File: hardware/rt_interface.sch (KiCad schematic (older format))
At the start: 51 parts, among them Q1 NTMFS5C682NL, Q2 NTMFS5C682NL, U1 NCS213, U2 MAX44246, U3 LM5109BSD

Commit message: Layout almost complete. Just needs a tidy.
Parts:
- removed JP1: SolderJumper_2_Open, station:SolderJumper-2_6A, symbol Jumper:SolderJumper_2_Open
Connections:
- net +V_PWR: now reaches C12.1, C13.1, C14.1, C15.1, C18.1, Q1.5 (D)
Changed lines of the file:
@@
 $Descr A4 11693 8268
 encoding utf-8
-Sheet 2 5
+Sheet 5 5
 Title ""
 Date ""
@@
 	7450 6100 7800 6100
 Connection ~ 7800 6100
-$Comp
-L power:+BATT #PWR013
-U 1 1 5EA17F06
-P 7450 3400
-AR Path="/5EA10576/5EA17F06" Ref="#PWR013"  Part="1"
-AR Path="/5EEA69D8/5EA17F06" Ref="#PWR?"  Part="1"
-AR Path="/5F6BFC9B/5EA17F06" Ref="#PWR?"  Part="1"
-AR Path="/5EFF2C78/5EA17F06" Ref="#PWR029"  Part="1"
-F 0 "#PWR029" H 7450 3250 50  0001 C CNN
-F 1 "+BATT" H 7465 3573 50  0000 C CNN
-F 2 "" H 7450 3400 50  0001 C CNN
-F 3 "" H 7450 3400 50  0001 C CNN
-	1    7450 3400
-	1    0    0    -1
-$EndComp
 $Comp
 L Device:C C12
@@
 	1300 1350 1300 1400
 Connection ~ 1300 1350
-$Comp
-L Jumper:SolderJumper_2_Open JP1
-U 1 1 5EEB1D69
-P 7450 3600
-AR Path="/5EA10576/5EEB1D69" Ref="JP1"  Part="1"
-AR Path="/5F6BFC9B/5EEB1D69" Ref="JP?"  Part="1"
-AR Path="/5EFF2C78/5EEB1D69" Ref="JP4"  Part="1"
-F 0 "JP4" V 7450 3668 50  0000 L CNN
-F 1 "SolderJumper_2_Open" V 7495 3668 50  0001 L CNN
-F 2 "station:SolderJumper-2_6A" H 7450 3600 50  0001 C CNN
-F 3 "~" H 7450 3600 50  0001 C CNN
-	1    7450 3600
-	0    1    1    0
-$EndComp
 Wire Wire Line
 	7450 3750 7450 3800
-Wire Wire Line
-	7450 3400 7450 3450
 $Comp
 L Device:C C17
@@
 Text Label 9700 5700 0    50   ~ 0
 SHUNT-
+$Comp
+L Station:+V_PWR #PWR051
+U 1 1 606EBBA2
+P 7450 3750
+AR Path="/5EFF2C78/606EBBA2" Ref="#PWR051"  Part="1"
+AR Path="/5EA10576/606EBBA2" Ref="#PWR050"  Part="1"
+F 0 "#PWR051" H 7450 3600 50  0001 C CNN
+F 1 "+V_PWR" H 7465 3923 50  0000 C CNN
+F 2 "" H 7450 3750 50  0001 C CNN
+F 3 "" H 7450 3750 50  0001 C CNN
+	1    7450 3750
+	1    0    0    -1
+$EndComp
 $EndSCHEMATC

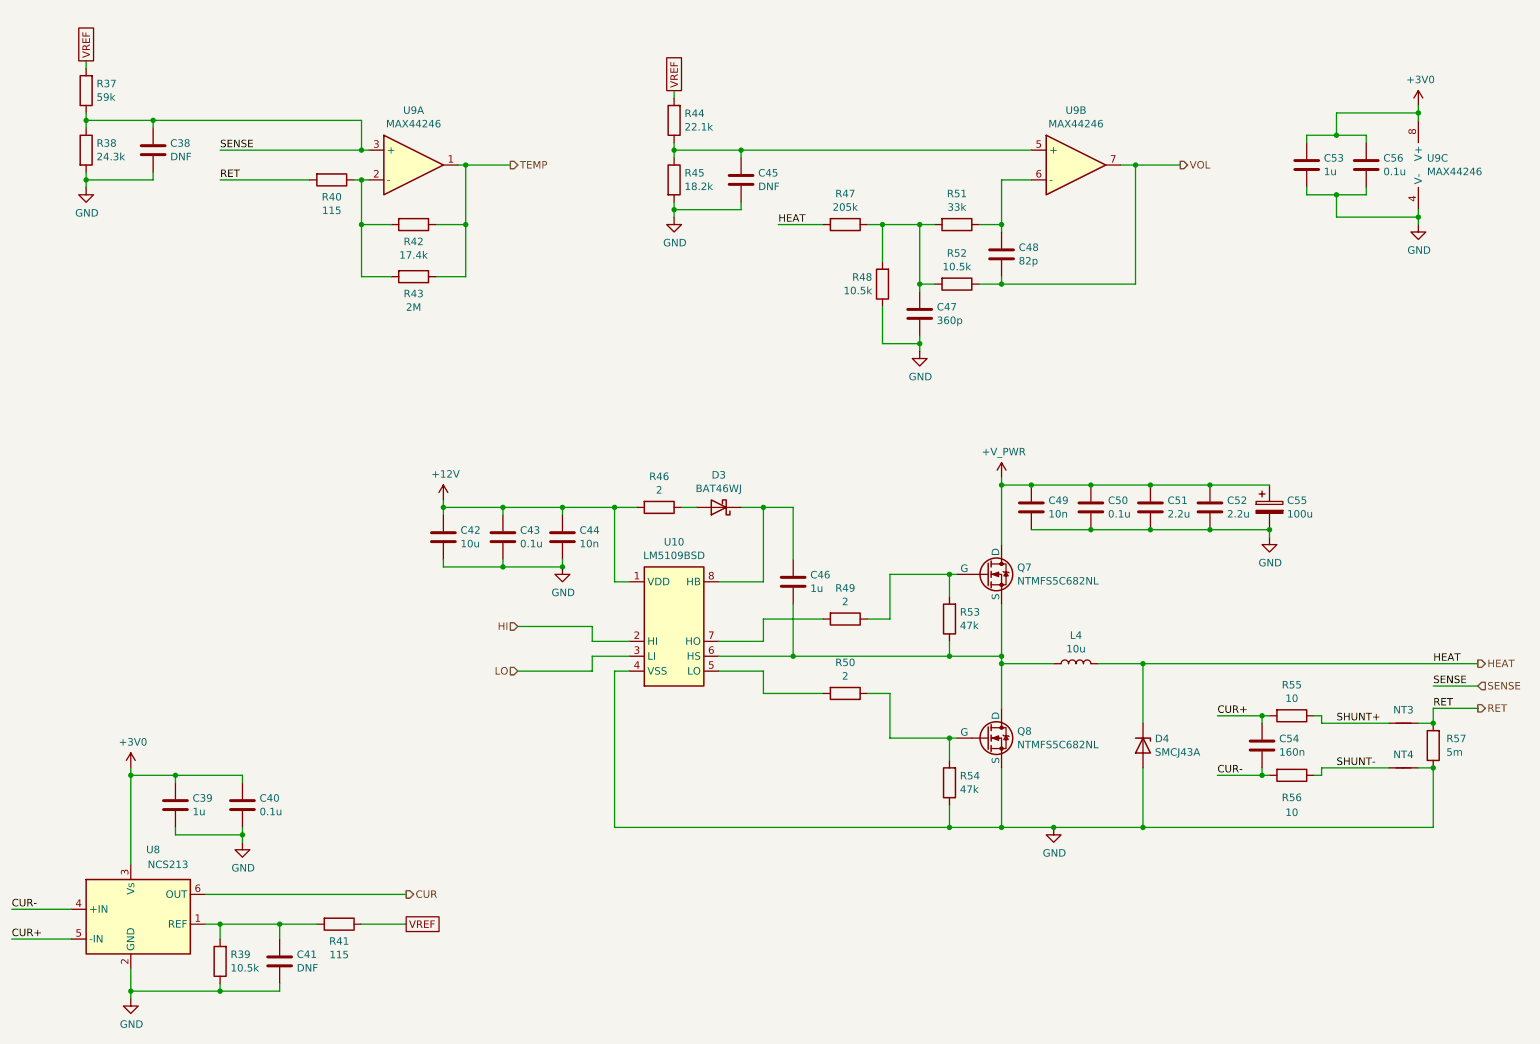
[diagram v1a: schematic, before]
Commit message: Update BOM * Datasheets * Manufacturers * Part numbers
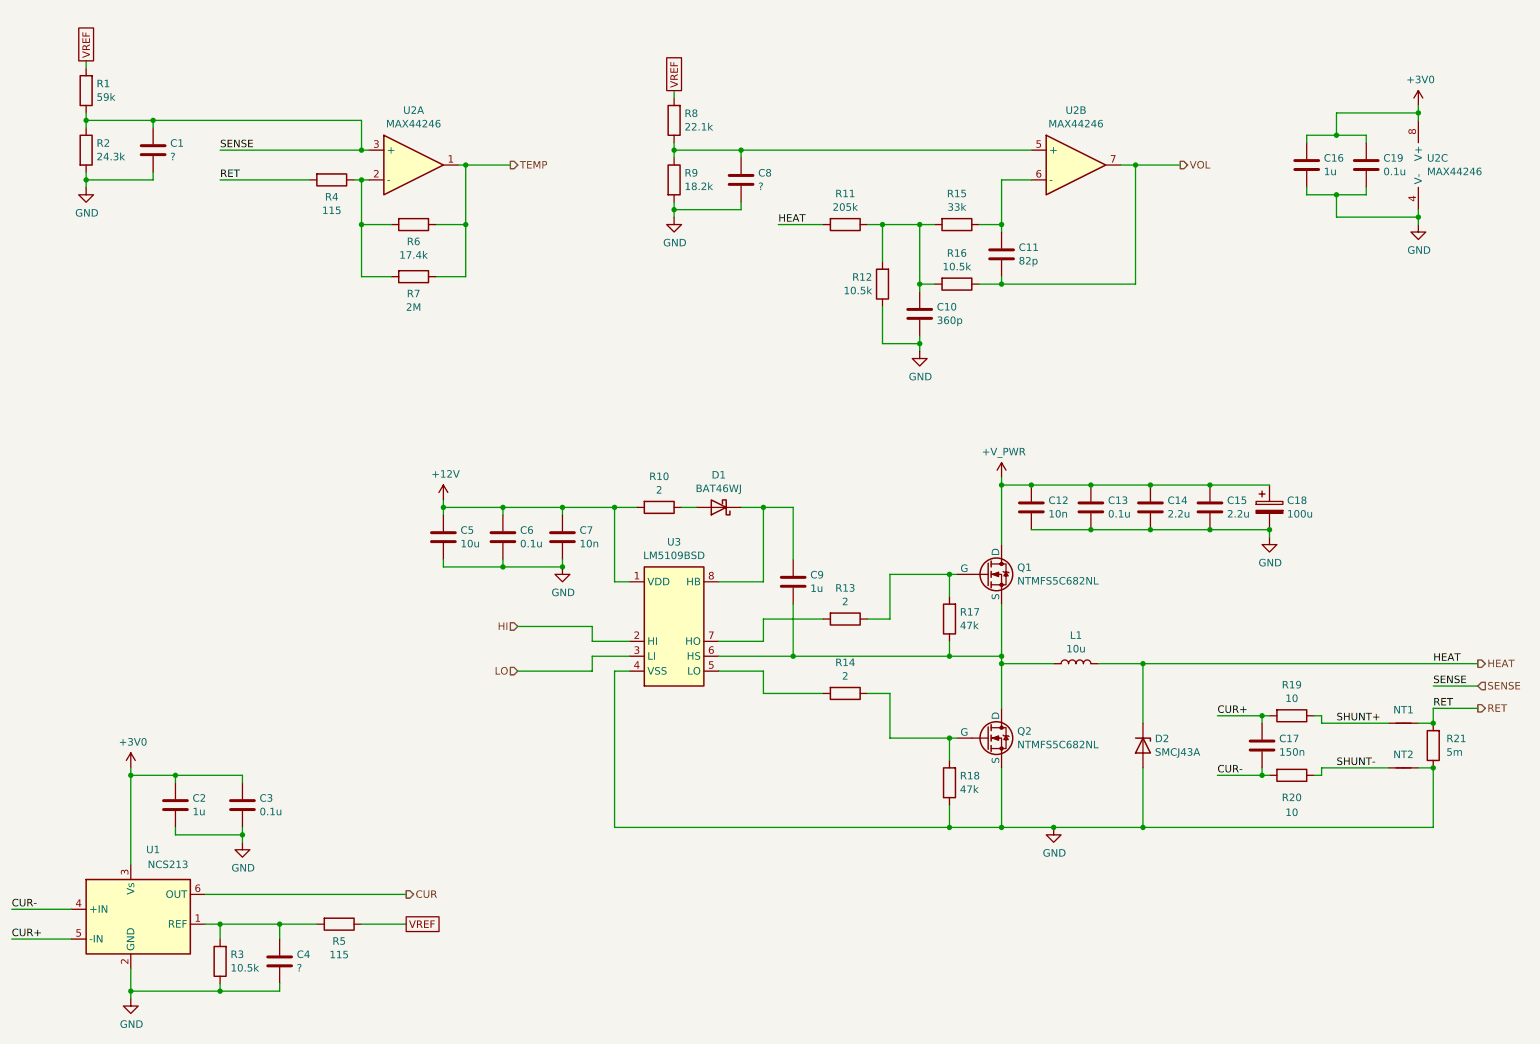
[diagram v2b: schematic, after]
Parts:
- C1, C4, C8: value DNF -> ?; DNP (none) -> X
- C10: Manufacturer (none) -> KEMET; Part Number (none) -> C0603C361J5GAC7867; Tolerance (none) -> 5%; Voltage Rating 25 V -> 50 V
- C11: Manufacturer (none) -> KEMET; Part Number (none) -> C0603C820J5GACTU; Tolerance (none) -> 5%; Voltage Rating 25 V -> 50 V
- C12: Manufacturer (none) -> TDK; Part Number (none) -> C1608X7R2A103K080AA; Tolerance (none) -> 10%
- C13: Manufacturer (none) -> Wurth Electronik; Part Number (none) -> 885012207128; Tolerance (none) -> 10%
- C14, C15: Manufacturer (none) -> Taiyo Yuden; Model C3225X7R2A225K230AB -> (none); Part Number (none) -> HMK325B7225KM-T; Tolerance (none) -> 10%
- C16, C2, C9: Manufacturer (none) -> KEMET; Part Number (none) -> C1206C105K3RACAUTO; Tolerance (none) -> 10%
- C17: value 160n -> 150n; Manufacturer (none) -> Wurth Electronik; Part Number (none) -> 885012206072; Tolerance (none) -> 10%
- C18: Manufacturer (none) -> Rubycon; Part Number (none) -> 63YXJ100M10X12.5; Tolerance (none) -> 20%
- C19, C3, C6: Manufacturer (none) -> Taiyo Yuden; Part Number (none) -> GMK107B7104KAHT; Tolerance (none) -> 10%
- C5: Manufacturer (none) -> Taiyo Yuden; Part Number (none) -> GMK316AB7106KL-TR; Tolerance (none) -> 10%
- C7: Manufacturer (none) -> TDK; Part Number (none) -> C1608X7R2A103K080AA; Tolerance (none) -> 10%; Voltage Rating 35 V -> 100 V
- D1: Manufacturer (none) -> Nexperia; Part Number (none) -> BAT46WJF
- D2: Manufacturer (none) -> Littelfuse; Part Number (none) -> SMCJ43A
- L1: Manufacturer (none) -> Bourns; Model SRP1265C-100M -> (none); Part Number (none) -> SRP1265C-100M
- NT1, NT2: DNP (none) -> X
- Q1, Q2: Manufacturer (none) -> ON Semiconductor; Part Number (none) -> NTMFS5C682NL
- R1: Manufacturer (none) -> Stackpole Electronics Inc; Part Number (none) -> RMCF0603FT59K0
- R10, R13, R14: Comments Need to be pulse rated? -> (none); Manufacturer (none) -> Panasonic; Part Number (none) -> ERJ-PA3J2R0V
- R11: Manufacturer (none) -> Stackpole Electronics Inc; Part Number (none) -> RMCF0603FT205K
- R12, R16, R3: Manufacturer (none) -> Stackpole Electronics Inc; Part Number (none) -> RMCF0603FT10K5
- R15: Manufacturer (none) -> Bourns; Part Number (none) -> CR0603-FX-3302ELF
- R17, R18: Manufacturer (none) -> Bourns; Part Number (none) -> CR0603-JW-473ELF
- R19, R20: Manufacturer (none) -> Bourns; Part Number (none) -> CR0603-FX-10R0ELF
- R2: Manufacturer (none) -> Stackpole Electronics Inc; Part Number (none) -> RMCF0603FT24K3
- R21: Manufacturer (none) -> Stackpole Electronics Inc; Part Number (none) -> CSRF0612FT5L00; Tolerance (none) -> 1%
- R4, R5: Manufacturer (none) -> Stackpole Electronics Inc; Part Number (none) -> RMCF0603FT115R
- R6: Manufacturer (none) -> Stackpole Electronics Inc; Part Number (none) -> RMCF0603FT17K4
- R7: Manufacturer (none) -> Panasonic; Part Number (none) -> ERJ-3EKF2004V
- R8: Manufacturer (none) -> Stackpole Electronics Inc; Part Number (none) -> RMCF0603FT22K1
- R9: Manufacturer (none) -> Stackpole Electronics Inc; Part Number (none) -> RMCF0603FT18K2
- U1: Manufacturer (none) -> ON Semiconductor; Part Number (none) -> NCS213RSQT2G
- U2: Manufacturer (none) -> Maxim; Part Number (none) -> MAX44246AUA+
- U3: Manufacturer (none) -> Texas Instruments; Part Number (none) -> LM5109BSD/NOPB
